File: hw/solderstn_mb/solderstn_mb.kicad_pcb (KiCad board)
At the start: 4 copper layers, 160 x 221.5 mm, 411 parts, among them J1201 Conn_02x05_Odd_Even, J1202 USB_B-TE_1734346-1, J1203 DB9_Male_MountingHoles, J1204 USB_A-CUI-UJ2-AH-1-SMT, J1205 Molex_NanoFit-1x02, J1301 SJ-3571N, J1302 Conn_02x05_Odd_Even, J201 74980104400, J2101 Conn_01x02, J2102 Molex_PicoBlade-53398-0271, J2103 CES-30207-158L120-67_Molex-Pi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, J2104 CES-703116-28PM_JST-conn, J2105 CES-30207-158L120-67_Molex-Pi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, J2106 CES-703116-28PM_JST-conn, J2107 Conn_Coaxial, J301 Molex_MicroFit_30-43045-0421, J501 FFC_conn_14p, J502 FFC_conn_14p, J503 JST_S2B-PH-SM4-TB, M501 FFC_retention_clamp, M502 FFC_retention_clamp, M601 Fan_4pin, M701 Fan_4pin, M801 Fan_4pin, Q1601 DMG1013T, Q1701 DMG1013T, Q1901 DMG1013T, Q2001 DMG1013T, Q2201 DMG1012T, Q301 Si4497DY, Q302 Si4497DY, Q303 DMG1012T, Q501 DMG1012T, Q601 DMG1012T, Q701 DMG1012T, Q801 DMG1012T, SW2201 Pushbutton_SMD_TS-1102W-4316, SW2202 Pushbutton_SMD_TS-1102W-4316, U1001 TMP100, U1101 TMP100, U1201 USBLC6-2SC6, U1202 74LVC2G17gw, U1203 USBLC6-2SC6, U1401 TMUX1219, U1402 TMUX1219, U1501 AD8552ARU, U1502 INA226, U1503 TPS2HB16AQ1, U1504 INA226, U1505 74LVC1G11dck, U1506 74LVC1G11dck, U1507 74LVC1G11dck, U1601 NE556d, U1602 74LVC1G175dck, U1603 74LVC1G11dck, U1701 74LVC1G175dck, U1702 74LVC1G11dck, U1801 AD8552ARU, U1802 INA226, U1803 TPS2HB16AQ1, U1804 INA226, U1805 74LVC1G11dck, U1806 74LVC1G11dck, U1807 74LVC1G11dck, U1901 NE556d, U1902 74LVC1G175dck, U1903 74LVC1G11dck, U2001 74LVC1G175dck, U2002 74LVC1G11dck, U201 IP101GA, U202 74LVC1G126SE, U2101 Si4735-D60-GU, U2102 TS4990IDT, U2103 TS4990IDT, U2201 MCP1316T-26LE-OT, U2202 W25Q64FV, U301 TPS54332DDA, U302 TLV1117LV30DCY, U303 TLV1117LV30DCY, U304 TLV1117LV30DCY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

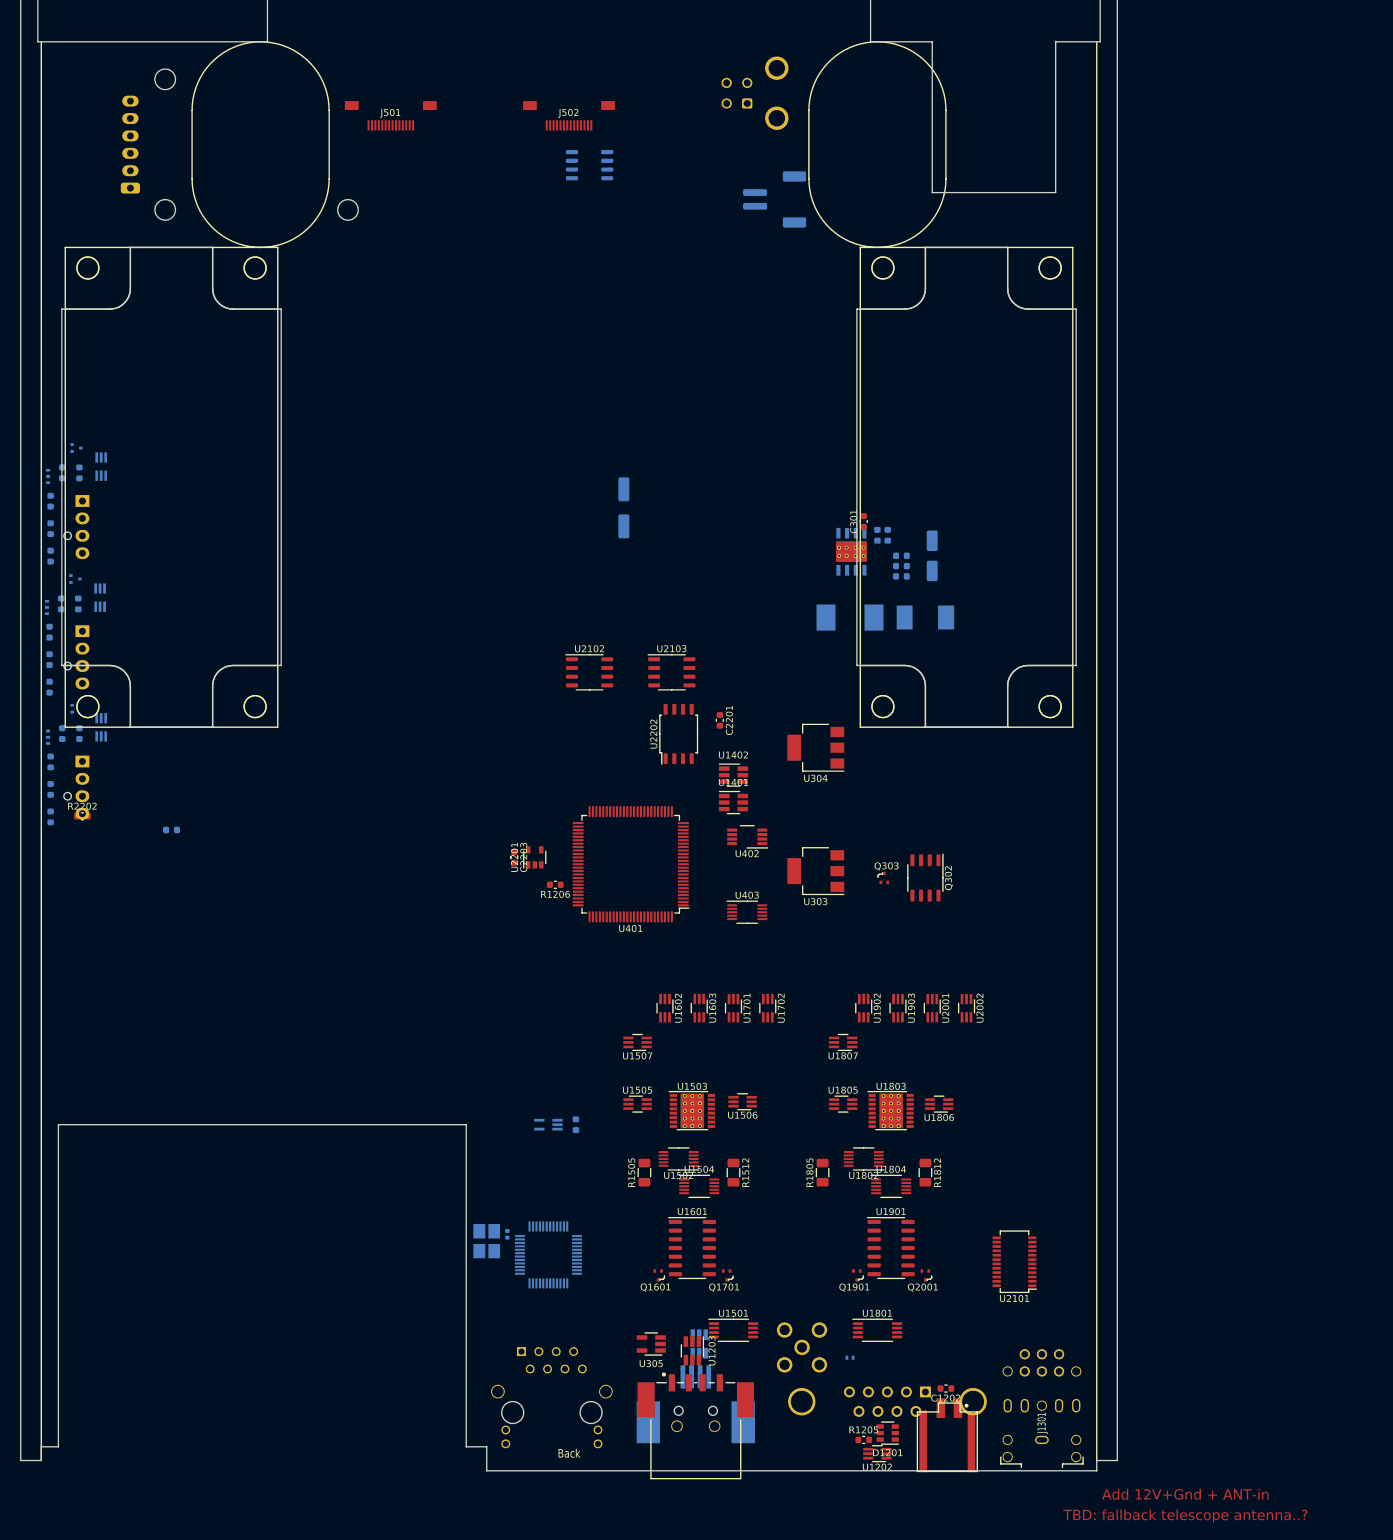
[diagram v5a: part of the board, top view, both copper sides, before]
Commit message: Updated MB cutouts, placements to new PSU-centered & 'mirrored' rearpanel layout. Schaffner FN283 (AC-inlet) now defaults to placed at inside rearpanel position -> rear looks (a bit) less cluttered
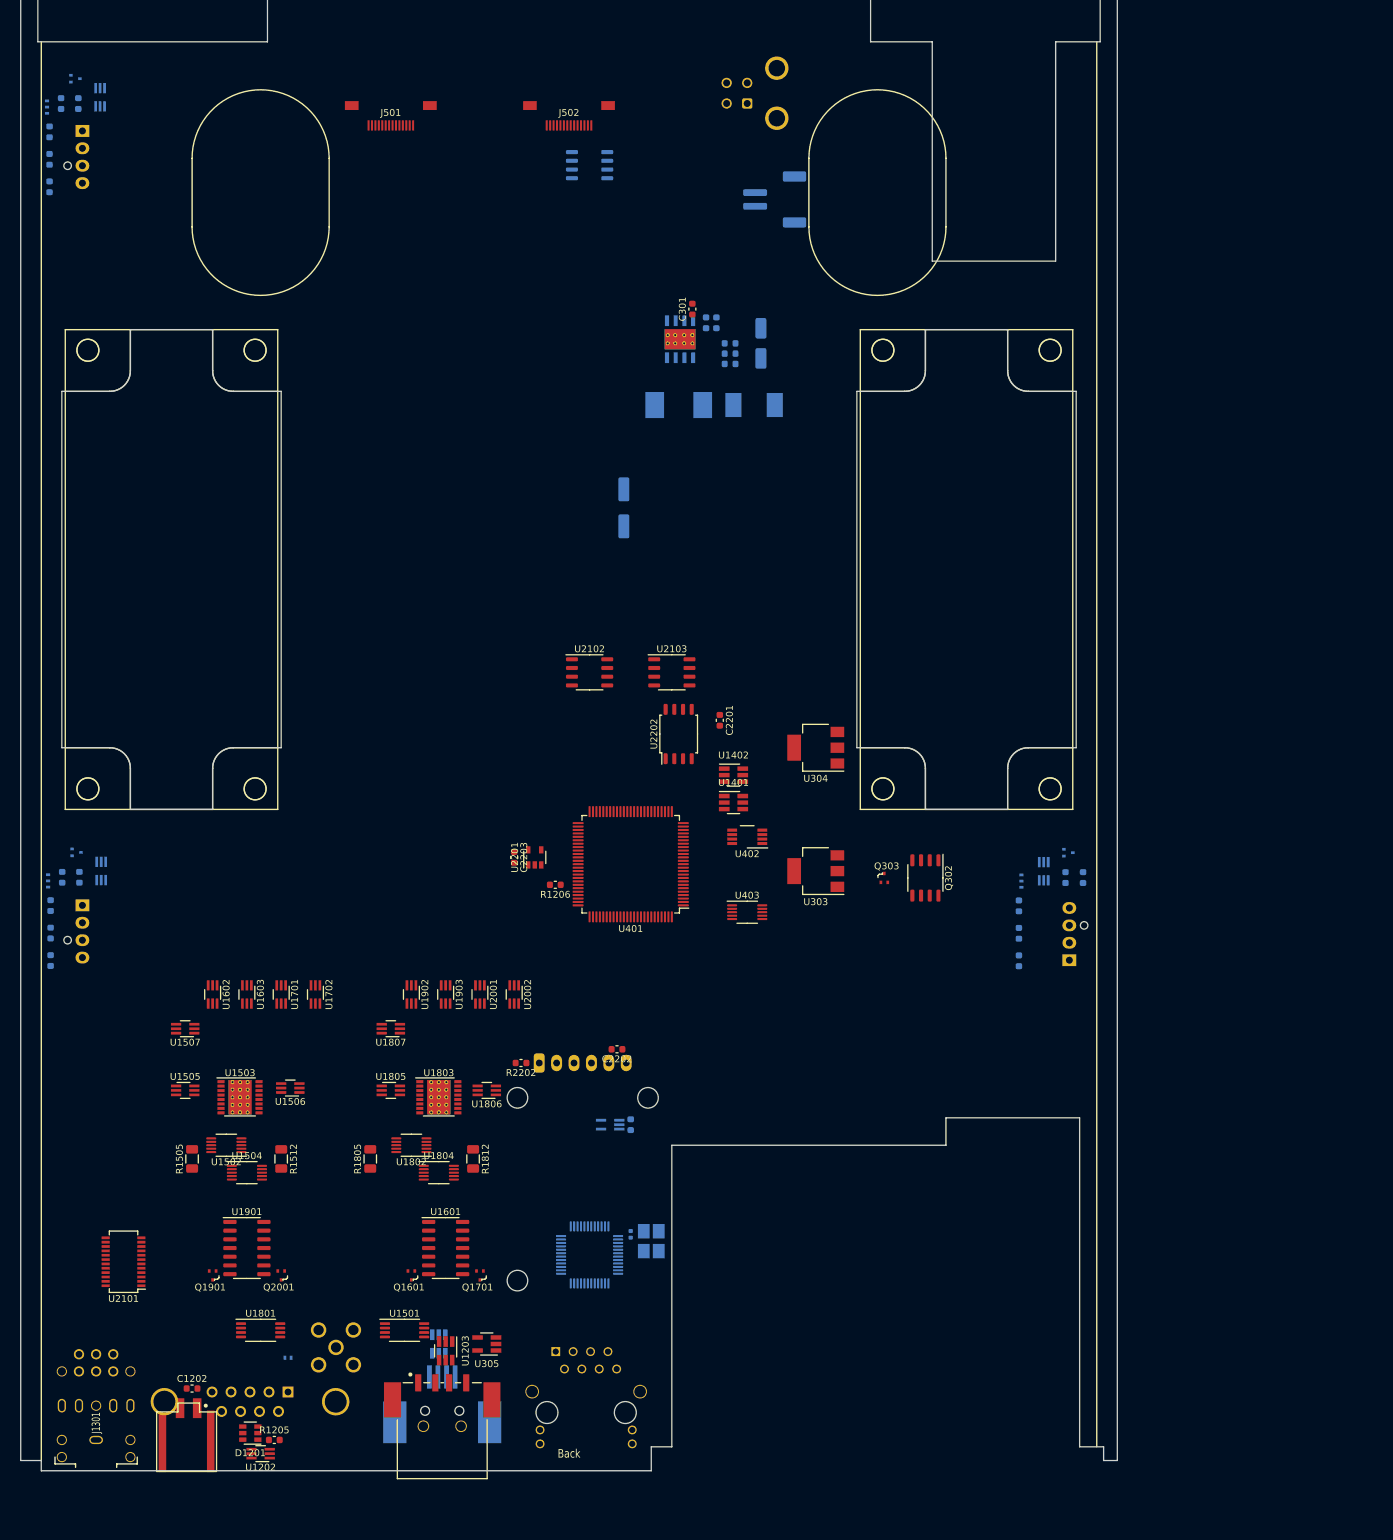
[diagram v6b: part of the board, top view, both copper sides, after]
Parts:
- C2202: moved to F.Cu
- moved R801 150.4 mm to (225.0, 164.9)
- moved RTC2201 149.4 mm to (152.0, 192.0), turned to 270 degrees
- moved M801 146.9 mm to (223.0, 177.0), turned to 90 degrees
- moved Q801 146.2 mm to (222.9, 161.3)
- moved C801 145.4 mm to (222.4, 164.9)
- moved JP801 143.5 mm to (216.0, 165.5)
- moved C802 142.8 mm to (215.6, 173.1)
- moved R802 142.8 mm to (215.6, 177.1)
- moved R803 142.8 mm to (215.6, 169.1)
- moved U801 139.1 mm to (219.3, 164.0)
- moved J1301 138.0 mm to (81.0, 242.0)
- moved U2101 130.0 mm to (85.0, 221.0)
- moved J1205 111.0 mm to (94.5, 247.5)
- moved C1202 110.0 mm to (95.0, 239.5), turned to 0 degrees
- moved Q1901 94.0 mm to (98.0, 223.0)
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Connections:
- J1203 pad 5: GND -> VCC
- J1203 pad 9: VCC -> GND
- J1205 pad 1: GND -> VIN
- J1205 pad 2: VIN -> GND
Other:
- outline, holes or cut-outs redrawn
- board text removed: "Add 12V+Gnd + ANT-in"
- board text removed: "TBD: fallback telescope antenna..?"

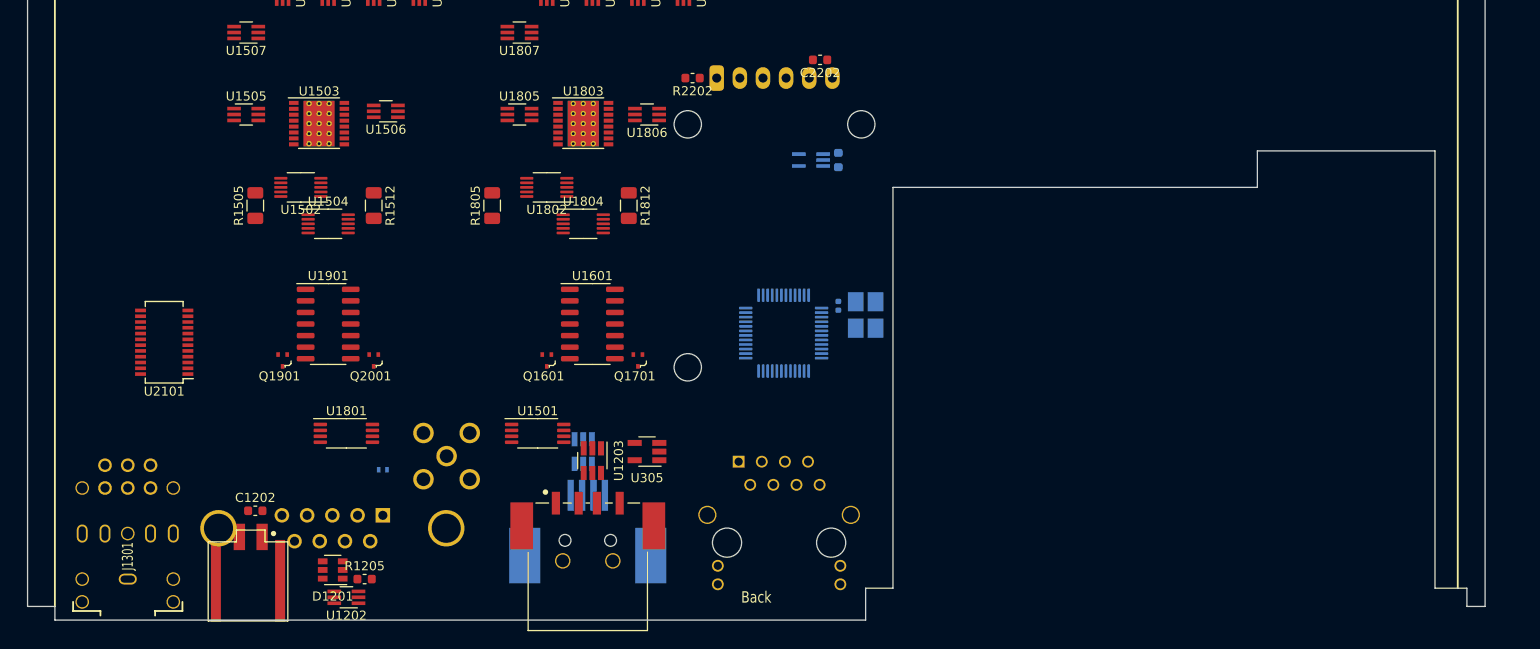
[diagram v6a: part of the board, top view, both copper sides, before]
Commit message: Minor re-alignments of rear-panel items that collided with box sides (SMA, outer DIN, Schaffner AC-in)
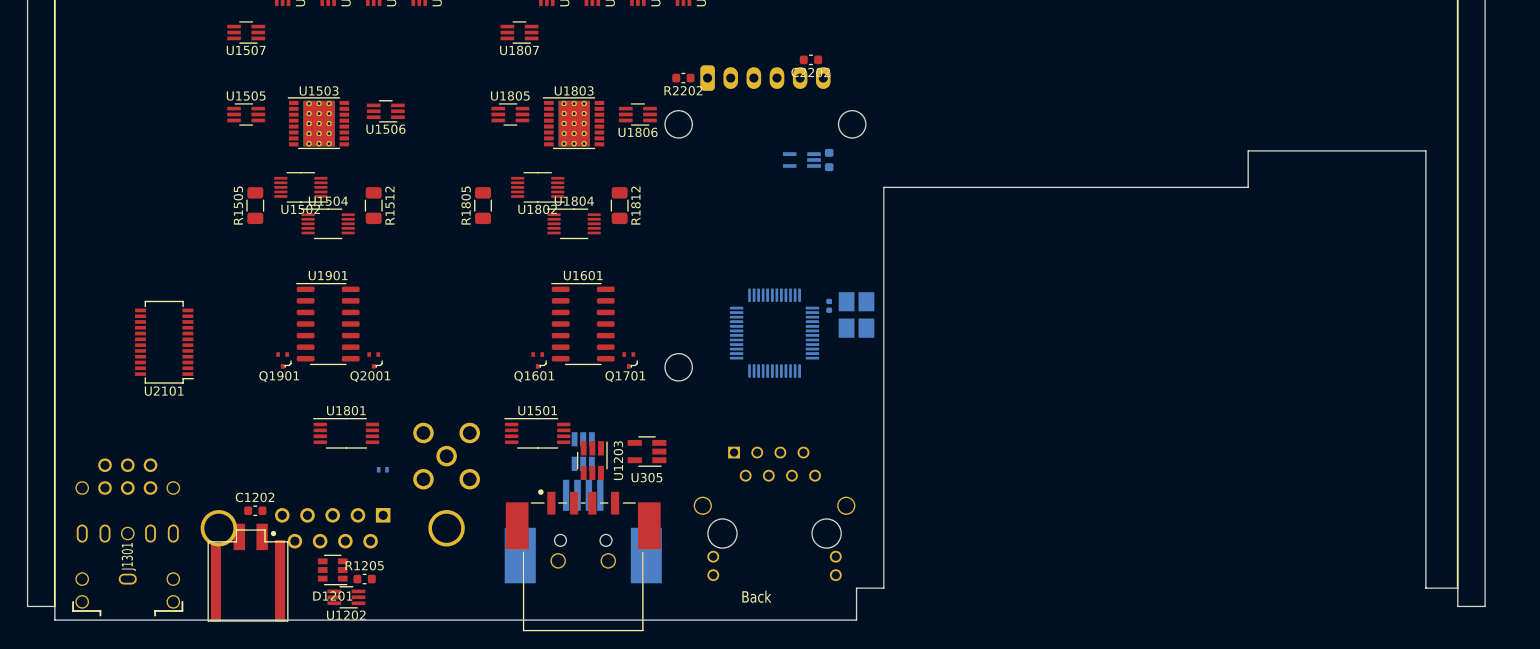
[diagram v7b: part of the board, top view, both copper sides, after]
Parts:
- moved J201 1.12 mm to (152.0, 242.0)
- moved C210 1.00 mm to (158.0, 201.0)
- moved C2202 1.00 mm to (156.0, 190.0)
- moved Q1601 1.00 mm to (126.0, 223.0)
- moved Q1701 1.00 mm to (136.0, 223.0)
- moved R1805 1.00 mm to (120.0, 206.0)
- moved R1812 1.00 mm to (135.0, 206.0)
- moved R210 1.00 mm to (158.0, 217.0)
- moved R2202 1.00 mm to (142.0, 192.0)
- moved RTC2201 1.00 mm to (151.0, 192.0)
- moved U1601 1.00 mm to (131.0, 219.0)
- moved U1802 1.00 mm to (126.0, 204.0)
- moved U1803 1.00 mm to (130.0, 197.0)
- moved U1804 1.00 mm to (130.0, 208.0)
- moved U1805 1.00 mm to (123.0, 196.0)
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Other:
- outline, holes or cut-outs redrawn
